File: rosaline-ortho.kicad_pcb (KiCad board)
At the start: 2 copper layers, 285.4 x 94.9 mm, 155 parts, among them J1 USB, J2 AVR_ISP_6, J3 JST, SW1 RESET, SW2 BOOT, U1 ATMEGA328-PU, Y1 16MHz

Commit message: Rename project
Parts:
- 2u_MX20, 2u_MX44: footprint juliet:MX_PCB_200H -> juliet:MX_PCB_200B
- moved REF** 6.19 mm to (235.7, 146.7)
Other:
- board text added: "Rosaline Ortho rev1.1 u/peejeh 08/2021"
- board text removed: "Juliet Ortho rev1 u/peejeh 08/2021"

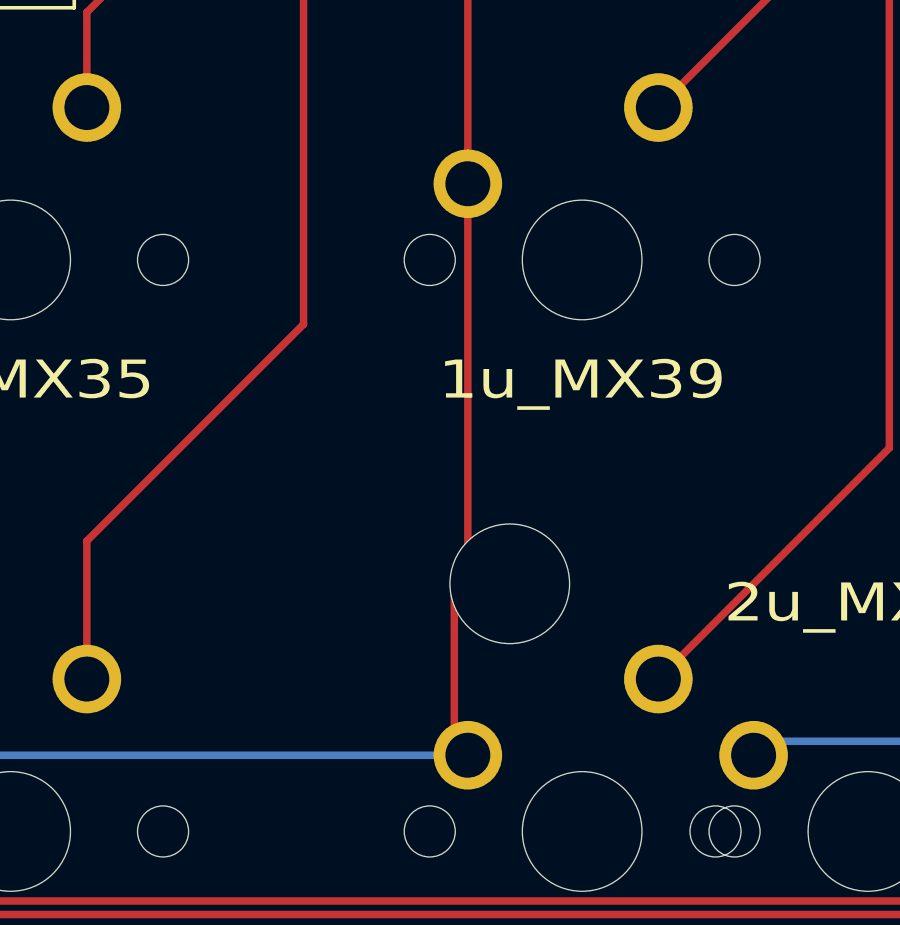
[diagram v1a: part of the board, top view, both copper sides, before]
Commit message: Fix broken trace on ortho PCB
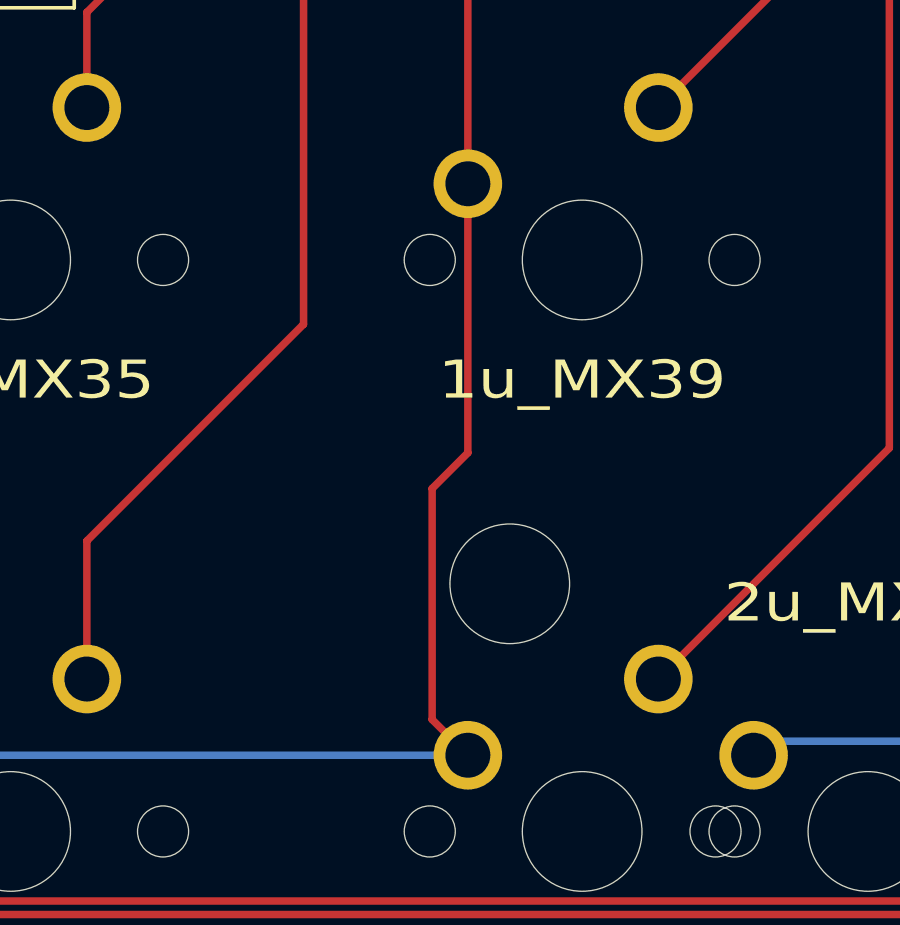
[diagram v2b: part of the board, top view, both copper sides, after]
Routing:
- net /COL4: track 181.9 -> 182.5 mm
